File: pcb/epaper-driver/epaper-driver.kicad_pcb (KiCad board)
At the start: 2 copper layers, 31.7 x 29.2 mm, 34 parts, among them J1 Main Conn, J2 Conn_01x24, J3 Conn_01x03_Pin, J4 Conn_01x03_Pin, J5 Conn_01x03_Pin, J8 SUPPORT, Q1 BSS138, Q2 AO3401A, Q3 S8050

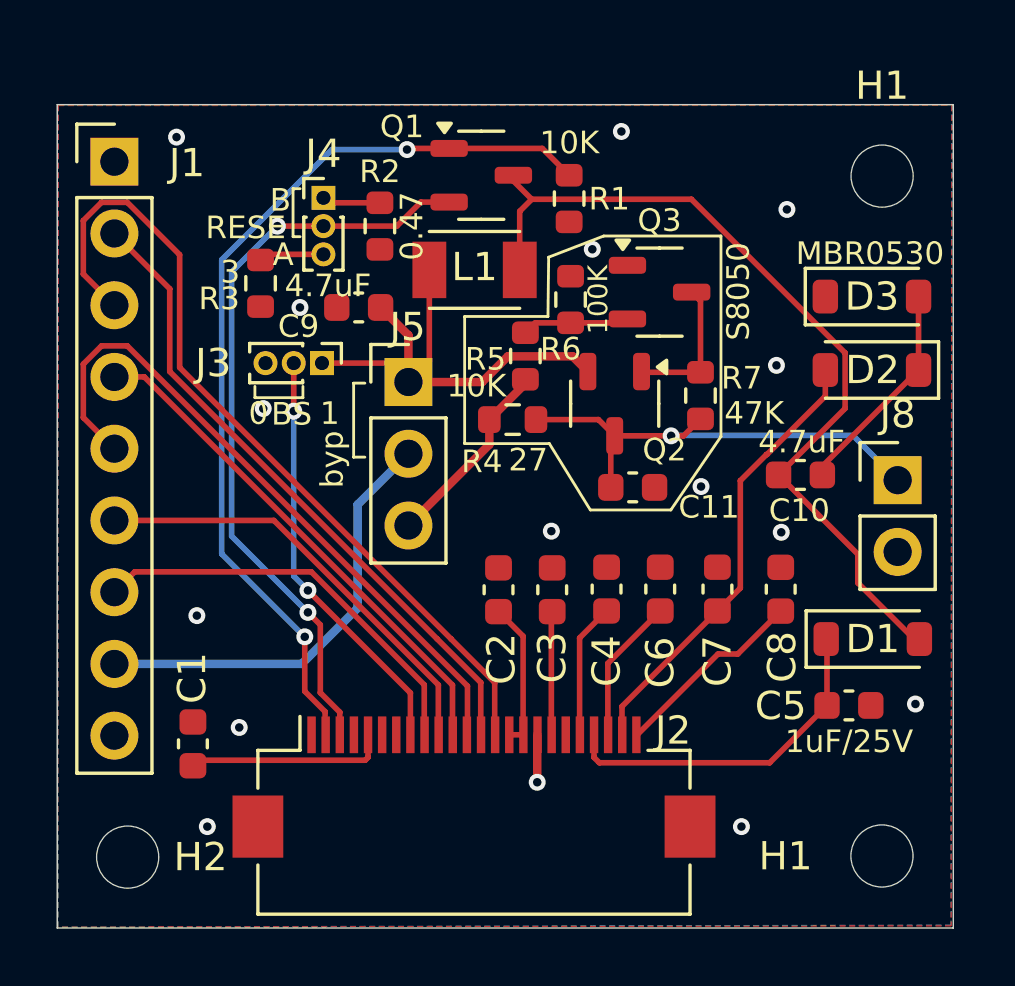
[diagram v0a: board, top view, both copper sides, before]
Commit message: [pcb] epaper-driver: mostly silkscreen size changes
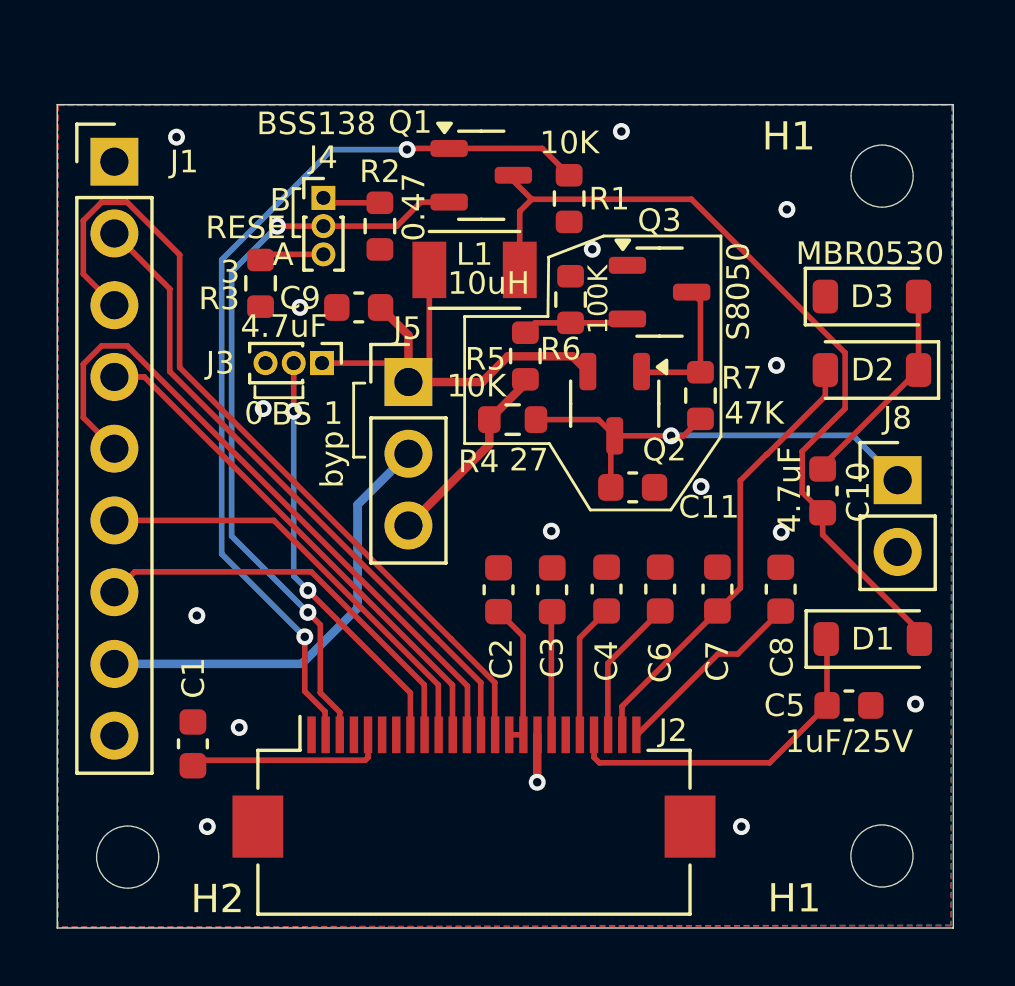
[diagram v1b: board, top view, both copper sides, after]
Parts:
- moved C10 0.97 mm to (168.0, 65.4), turned to 90 degrees
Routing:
- net Net-(D1-A): track 30.4 -> 29.6 mm
